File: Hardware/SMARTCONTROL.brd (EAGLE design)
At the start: 40 x 50 mm, 37 parts, among them IC1 ESP12-SMT, Q2 RJU003N03, Q3 RJU003N03, Q4 RJU003N03, Q5 RJU003N03

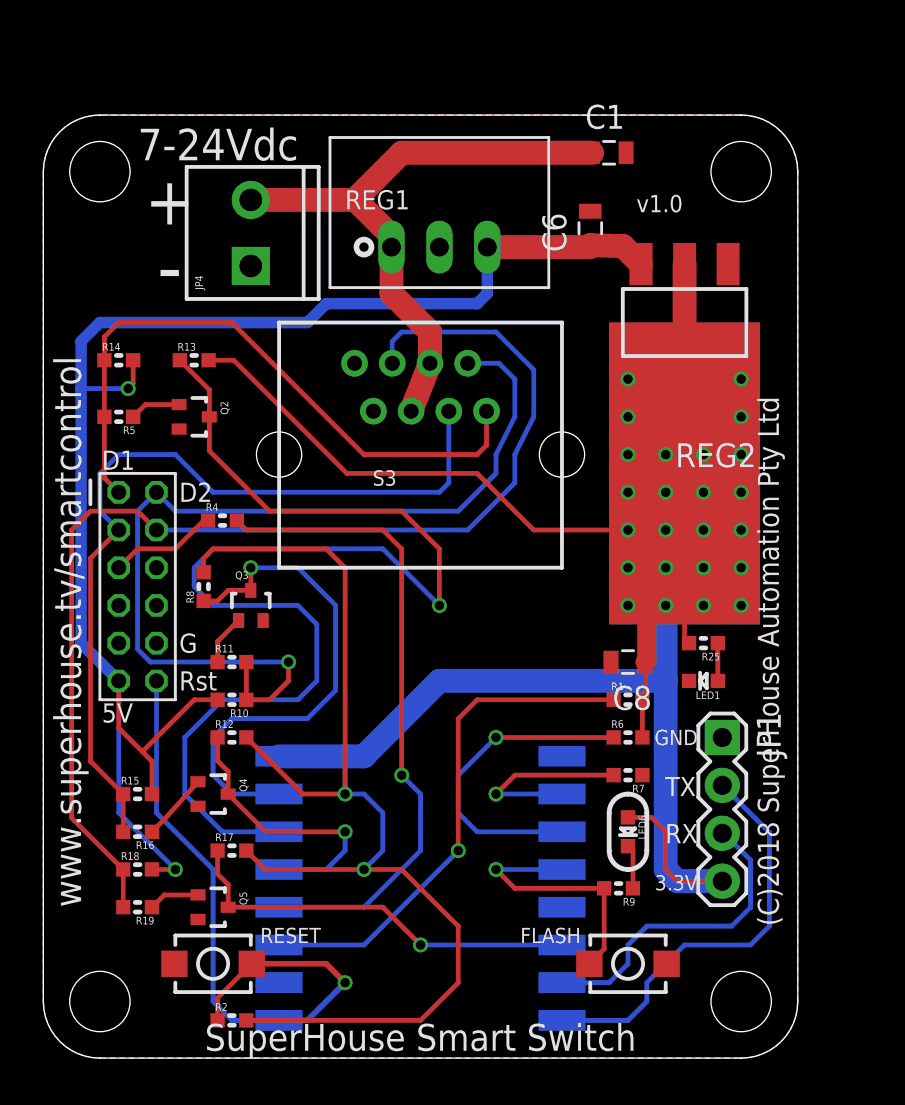
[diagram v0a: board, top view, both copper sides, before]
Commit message: Replaced 3.3V regulator. Switched button1 and LED pins. Extended PCB to improve bolt clearance. Changed bottom layer to 3.3V.
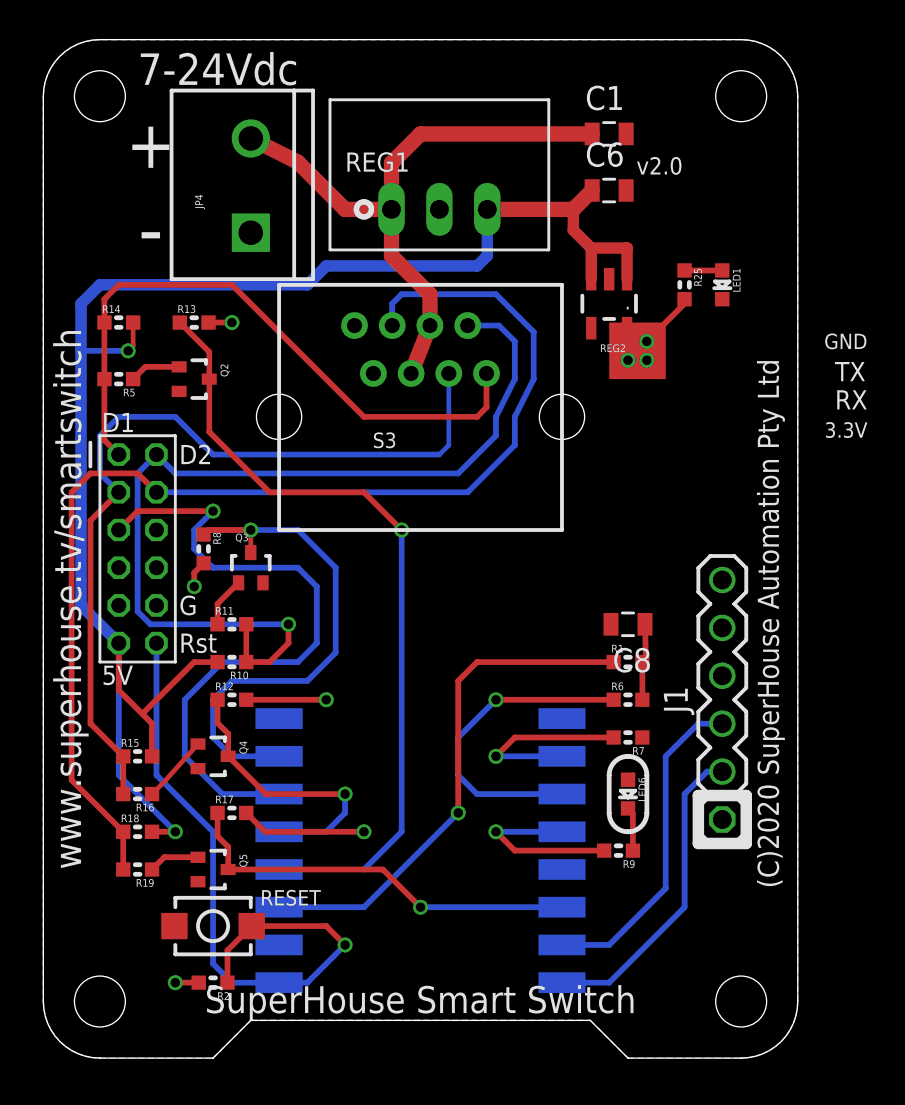
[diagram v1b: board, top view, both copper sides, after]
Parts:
- removed JP1: (no value), freetronics-jon:1X04
- removed R4: 100R, SuperHouse-DiscreteSemi:R0603
- removed S2: FLASH, SuperHouse-Switches:TACTILE_SMD_3X4X2
- added J1: ESPFLASH-1X6-2.54-SOCKET, SuperHouse-ESPFlash:1X6-2.54-SOCKET
- JP4: device freetronics-jon:SCREWTERMINAL-3.5MM-2 -> SuperHouse-Connectors:SCREWTERMINAL-5MM-2
- REG2: value LD111733 -> AP2112KSOT25; device SuperHouse-Regulators:SOT-223 -> SuperHouse-Regulators:SOT23-5
- moved LED1 21.0 mm to (36.0, 41.0), turned to 270 degrees
- moved R25 19.0 mm to (34.0, 41.0), turned to 270 degrees
- moved JP4 4.30 mm to (11.0, 46.3)
- moved REG2 4.12 mm to (30.0, 40.0)
- moved C6 2.24 mm to (30.0, 46.0), turned to 0 degrees
- moved R2 2.24 mm to (9.00, 4.00), turned to 180 degrees
- moved C8 2.00 mm to (31.0, 23.0)
- moved H1 2.00 mm to (4.00, 32.0)
- moved IC1 2.00 mm to (20.0, 8.00)
- moved LED6 2.00 mm to (31.0, 14.0)
- moved Q2 2.00 mm to (8.00, 36.0)
- moved Q3 2.00 mm to (11.0, 26.0)
- moved Q4 2.00 mm to (9.00, 16.0)
- moved Q5 2.00 mm to (9.00, 10.0)
- moved R1 2.00 mm to (31.0, 21.0)
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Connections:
- removed net LEDS: H1.5, R4.1
- removed net RESET: H1.12, IC1.1, R2.1, S1.1
- removed net RX: IC1.15, JP1.3
- removed net TX: IC1.16, JP1.2
- new net !RESET: H1.12, IC1.1, J1.5, R2.1, S1.1
- new net ESP_RX: IC1.15, J1.3
- new net ESP_TX: IC1.16, J1.2
- net 3.3V: now also J1.4, REG2.5; no longer JP1.4, REG2.2, REG2.4
- net 5V: now also REG2.1
- net GND: now also J1.1, REG2.2; no longer JP1.1, REG2.1, S2.1
- net GPIO0: now also J1.6; no longer S2.2
- net GPIO12: now also H1.5; no longer Q2.3, R13.1
- net GPIO16: now also Q2.3, R13.1; no longer R4.2
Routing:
- net 3.3V: track 221.3 -> 23.6 mm, vias 26 -> 8
- net RESET: track 35.6 -> 0.00 mm, vias 1 -> 0
- net !RESET: track 0.00 -> 35.4 mm, vias 0 -> 1
- net GPIO12: track 65.9 -> 35.2 mm
- net TX: track 22.2 -> 0.00 mm
- net ESP_RX: track 0.00 -> 17.5 mm
- net RX: track 16.8 -> 0.00 mm
- net ESP_TX: track 0.00 -> 16.6 mm
- net GPIO16: track 34.5 -> 42.1 mm
- net LEDS: track 5.77 -> 0.00 mm
- net 5V: track 80.9 -> 85.9 mm
- net GPIO0: track 14.0 -> 9.65 mm
- added copper zone on layer 16, net 3.3V
- removed copper zone on layer 16, net GND
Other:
- board size 40 x 50 mm -> 40 x 54 mm
- board text added: "(C)2020 SuperHouse Automation Pty Ltd"
- board text added: "v2.0"
- board text added: "www.superhouse.tv/smartswitch"
- board text removed: "(C)2018 SuperHouse Automation Pty Ltd"
- board text removed: "FLASH"
- board text removed: "v1.0"
- board text removed: "www.superhouse.tv/smartcontrol"

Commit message: Routing for expanded PCB.
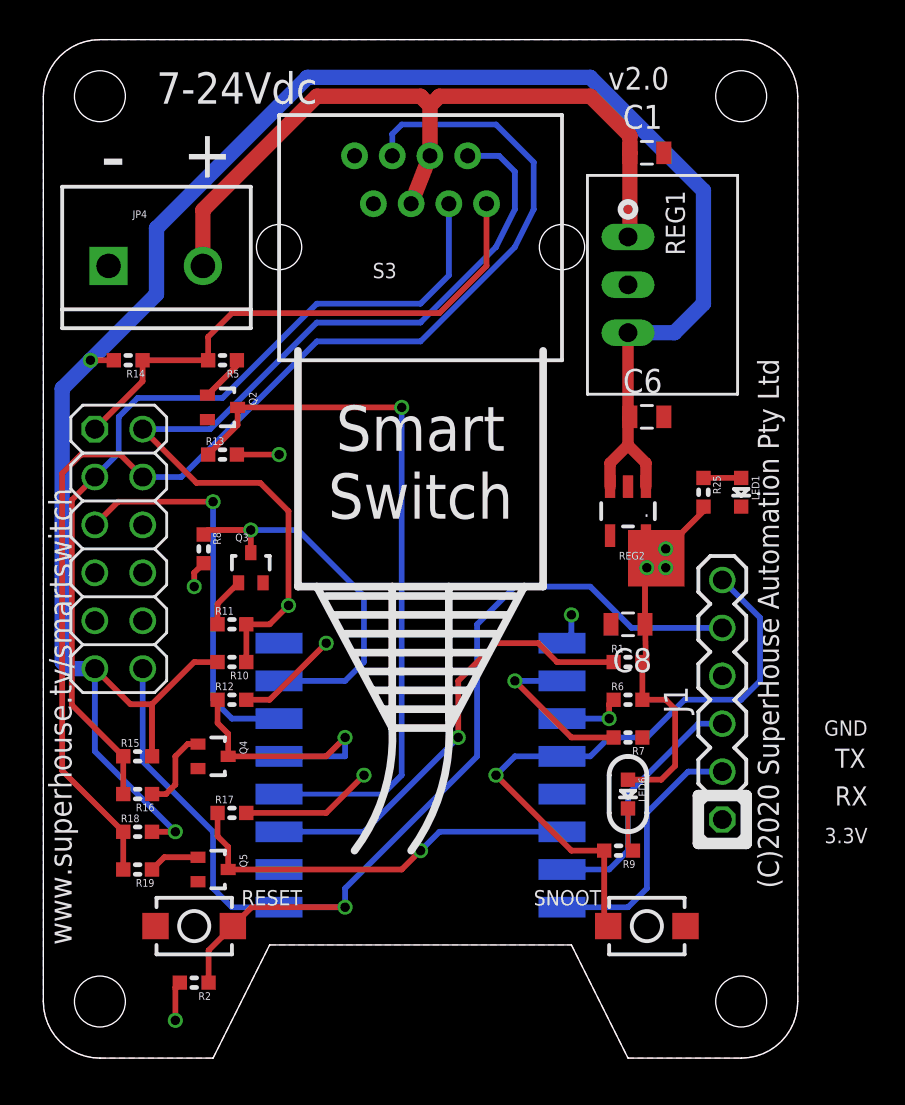
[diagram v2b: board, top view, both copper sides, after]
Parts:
- added S2: FLASH, SuperHouse-Switches:TACTILE_SMT_3X4X2
- H1: value M06X22MM -> M02X6-PIN-BELOW; device freetronics-jon:2X6-2MM -> SuperHouse-Connectors:2X06-P-BELOW
- S1: device SuperHouse-Switches:TACTILE_SMD_3X4X2 -> SuperHouse-Switches:TACTILE_SMT_3X4X2
- S3: value RJ45 -> RJ45-PLASTIC
- moved C6 12.2 mm to (32.0, 34.0)
- moved LED1 11.0 mm to (37.0, 30.0)
- moved R25 11.0 mm to (35.0, 30.0)
- moved REG2 11.0 mm to (31.0, 29.0)
- moved REG1 10.8 mm to (31.0, 41.0), turned to 270 degrees
- moved S3 9.00 mm to (20.0, 43.0)
- moved R13 7.16 mm to (9.50, 32.0)
- moved JP4 6.59 mm to (6.00, 42.0), turned to 0 degrees
- moved R5 5.59 mm to (9.50, 37.0)
- moved H1 5.00 mm to (4.00, 27.0), turned to 270 degrees
- moved IC1 4.00 mm to (20.0, 12.0)
- moved C1 2.24 mm to (32.0, 48.0)
- moved Q2 2.12 mm to (9.50, 34.5)
- moved R14 2.06 mm to (4.50, 37.0), turned to 180 degrees
- moved R2 1.00 mm to (8.00, 4.00)
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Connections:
- net GND: now also S2.1
- net GPIO0: now also S2.2
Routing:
- net !RESET: track 35.4 -> 63.5 mm
- net GPIO0: track 9.65 -> 33.7 mm
- net 5V: track 85.9 -> 107.5 mm
- net GPIO12: track 35.2 -> 21.2 mm
- net 3.3V: track 23.6 -> 37.6 mm
- net GPIO2: track 17.0 -> 3.60 mm
- net 12V: track 32.3 -> 40.2 mm
- net GPIO13: track 27.1 -> 19.7 mm
- net BUTTON1: track 34.0 -> 29.0 mm
- net BUTTON4: track 62.4 -> 66.7 mm
- net ESP_RX: track 17.5 -> 13.5 mm
- net GPIO16: track 42.1 -> 38.3 mm
- net CH_PD: track 27.2 -> 24.1 mm
- net ESP_TX: track 16.6 -> 13.8 mm
- net BUTTON3: track 44.5 -> 46.6 mm
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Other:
- outline, holes or cut-outs redrawn
- board text added: "SNOOT"
- board text added: "Smart Switch"
- board text removed: "5V"
- board text removed: "D1"
- board text removed: "D2"
- board text removed: "G"
- board text removed: "Rst"
- board text removed: "SuperHouse Smart Switch"

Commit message: Moved v2 board back to original name, and finished ERC/DRC for v2.0 release.
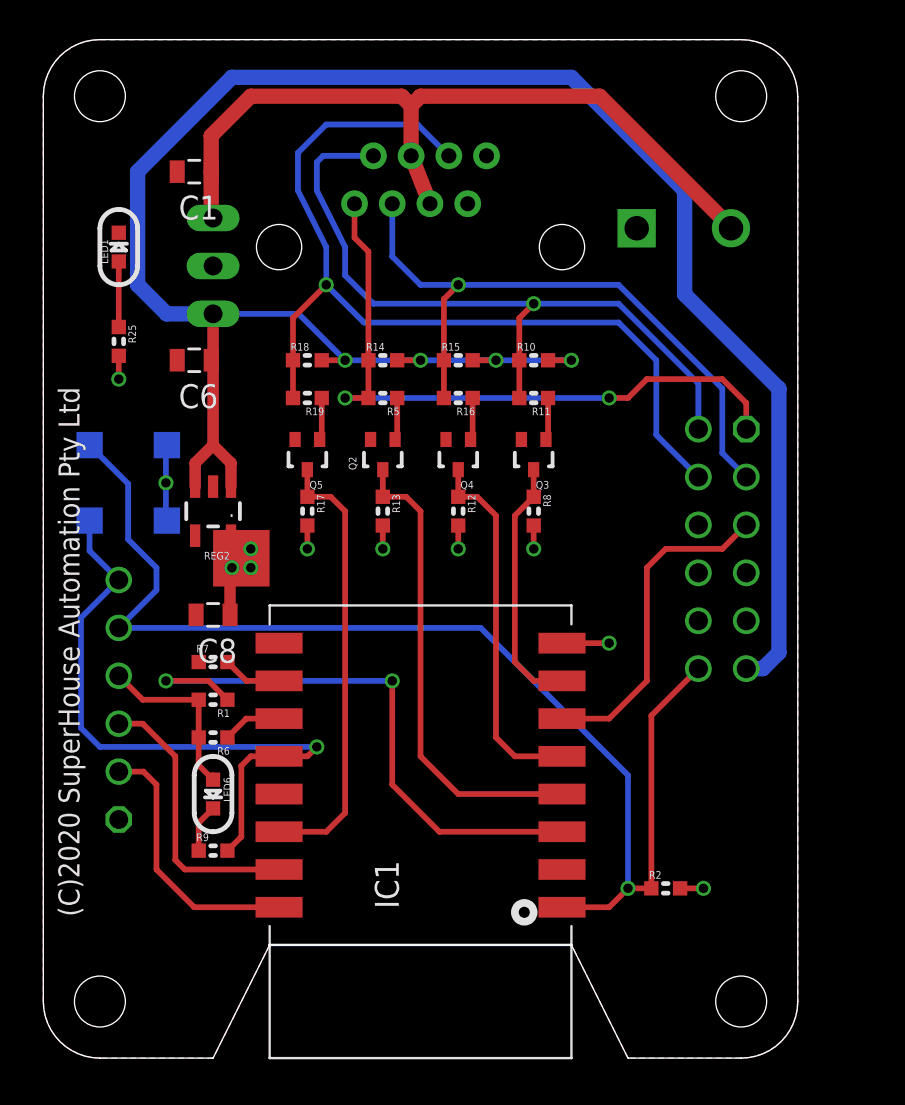
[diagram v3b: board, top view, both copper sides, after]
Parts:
- moved LED1 35.5 mm to (4.00, 43.0), turned to 90 degrees
- moved S2 34.9 mm to (4.50, 28.5), flipped to the bottom, turned to 0 degrees
- moved R25 32.0 mm to (4.00, 38.0)
- moved H1 32.0 mm to (36.0, 27.0), flipped to the bottom
- moved J1 32.0 mm to (4.00, 19.0), flipped to the bottom
- moved JP4 28.1 mm to (34.0, 44.0), flipped to the bottom, turned to 180 degrees
- moved R15 27.0 mm to (22.0, 37.0)
- moved R16 27.0 mm to (22.0, 35.0)
- moved R18 26.6 mm to (14.0, 37.0)
- moved R19 26.6 mm to (14.0, 35.0)
- moved S1 25.7 mm to (4.50, 32.5), flipped to the bottom
- moved R2 25.5 mm to (33.0, 9.00), turned to 0 degrees
- moved C6 24.2 mm to (8.00, 37.0), turned to 180 degrees
- moved C1 24.0 mm to (8.00, 47.0), turned to 180 degrees
- moved R10 22.6 mm to (26.0, 37.0), turned to 0 degrees
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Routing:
- net BUTTON4: track 66.7 -> 49.7 mm, vias 0 -> 1
- net GPIO16: track 38.3 -> 25.1 mm, vias 1 -> 0
- net 3.3V: track 37.6 -> 25.5 mm, vias 8 -> 10
- net BUTTON3: track 46.6 -> 34.7 mm, vias 0 -> 1
- net BUTTON2: track 49.0 -> 38.3 mm
- net CH_PD: track 24.1 -> 31.2 mm, vias 1 -> 2
- net BUTTON1: track 29.0 -> 35.4 mm, vias 0 -> 2
- net GPIO13: track 19.7 -> 13.5 mm, vias 1 -> 0
- net GPIO15: track 8.98 -> 3.15 mm, vias 1 -> 0
- net GPIO14: track 14.3 -> 19.5 mm, vias 1 -> 0
- net GPIO12: track 21.2 -> 17.5 mm, vias 1 -> 0
- net 5V: track 107.5 -> 110.1 mm, vias 2 -> 4
- net !RESET: track 63.5 -> 66.1 mm
- net GND: track 1.71 -> 4.11 mm
- net N$3: track 4.41 -> 2.25 mm
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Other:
- board text added: "3V3"
- board text added: "ESPFlash"
- board text added: "ESP_RX"
- board text added: "ESP_TX"
- board text added: "IO0"
- board text added: "RST"
- board text removed: "3.3V"
- board text removed: "RX"
- board text removed: "TX"
